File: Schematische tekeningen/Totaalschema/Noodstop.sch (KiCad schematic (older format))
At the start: 19 parts, among them J8 Noodstop, Q4 BS170, Q5 BS170, U11 PC817, U12 PC817, U13 74AHC1G32

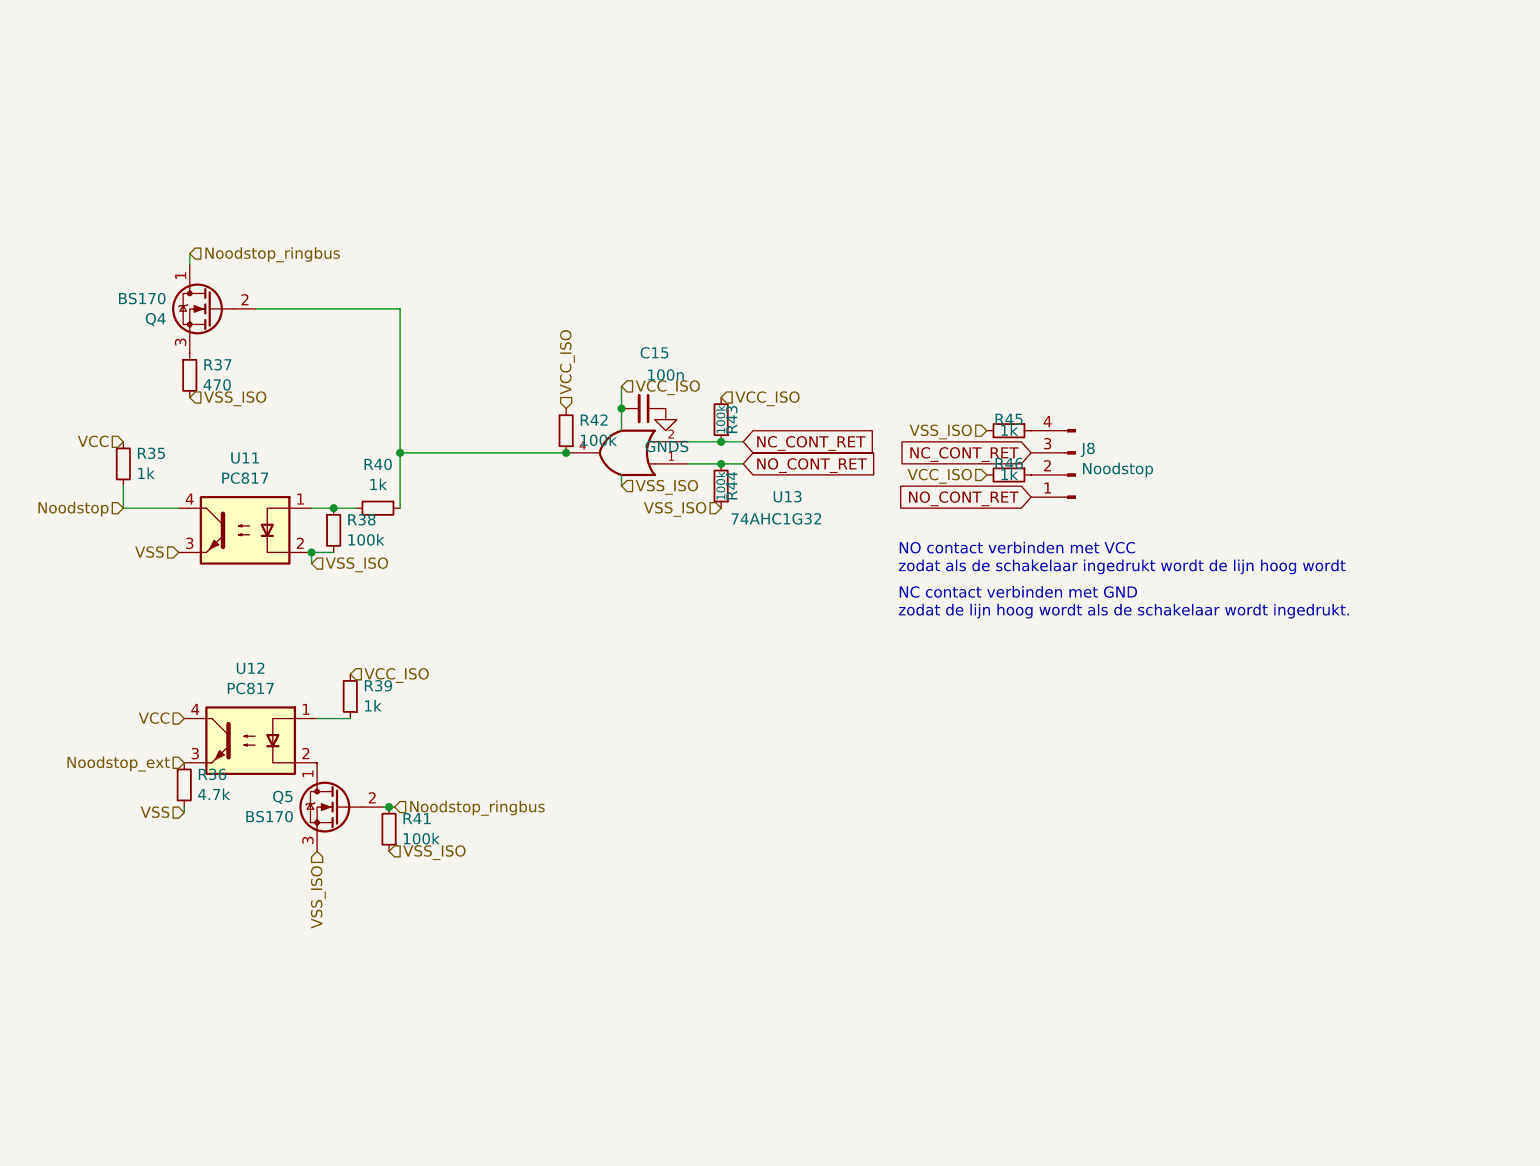
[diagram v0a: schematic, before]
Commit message: Footprints aangepast. Tekening aangepast
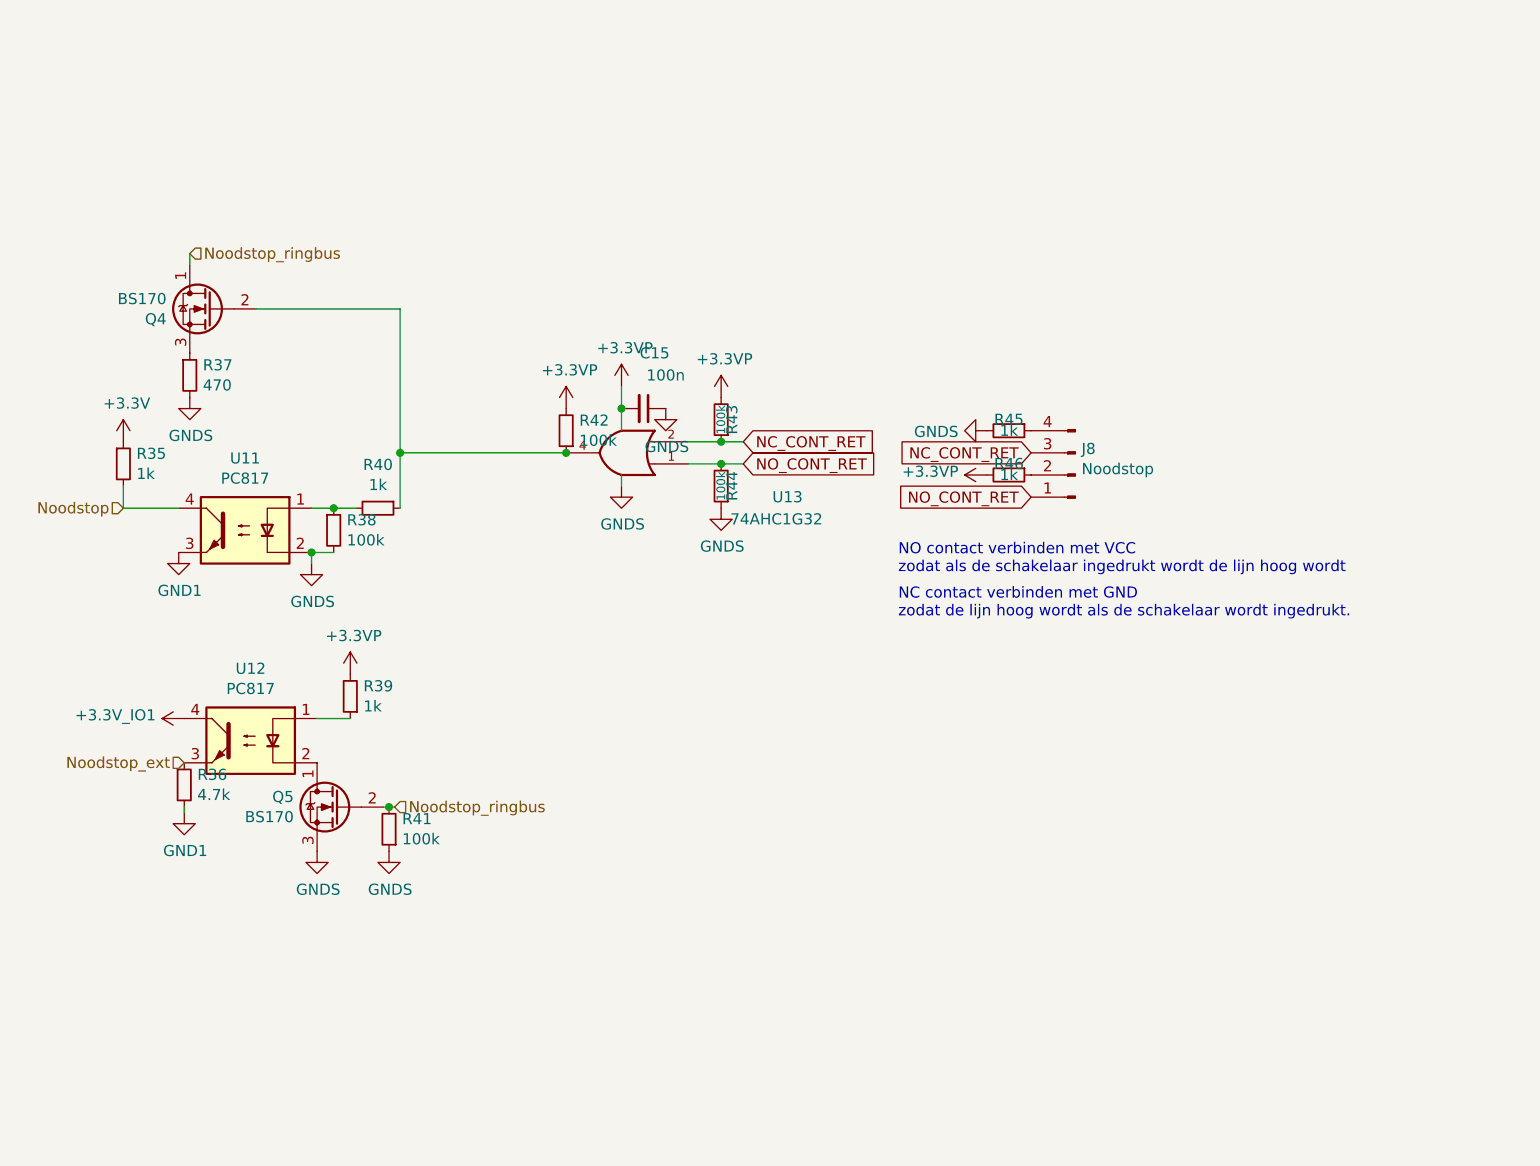
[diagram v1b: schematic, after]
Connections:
- net GNDS: now also Q5.3 (S), R37.2, R38.2, R41.1, R44.1, R45.2, U11.2, U13.5 (VCC)
- net GND renamed +3.3VP
- removed net VCC: Q5.3 (S), R35.1, R37.2, R38.2, R41.1, R44.1, R45.2, U11.2, U12.4, U13.5 (VCC)
- net VSS renamed GND1
- new net +3V3: R35.1
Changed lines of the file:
@@
 $Descr A4 11693 8268
 encoding utf-8
-Sheet 5 5
+Sheet 4 5
 Title ""
 Date ""
@@
 	0    1    1    0
 $EndComp
-Wire Wire Line
-	6250 3000 6250 3100
 Connection ~ 6250 3100
 Wire Wire Line
@@
 Text HLabel 4000 3550 0    50   Input ~ 0
 Noodstop
-Text HLabel 4250 3750 0    50   Input ~ 0
-VSS
-Text HLabel 4850 3800 2    50   Input ~ 0
-VSS_ISO
-Text HLabel 6250 3450 2    50   Input ~ 0
-VSS_ISO
 Wire Wire Line
 	6250 3450 6250 3400
-Text HLabel 6250 3000 2    50   Input ~ 0
-VCC_ISO
-Text HLabel 6700 3050 2    50   Input ~ 0
-VCC_ISO
-Text HLabel 7900 3400 0    50   Input ~ 0
-VCC_ISO
-Text HLabel 7900 3200 0    50   Input ~ 0
-VSS_ISO
-Text HLabel 4300 3050 2    50   Input ~ 0
-VSS_ISO
-Text HLabel 4000 3250 0    50   Input ~ 0
-VCC
 Text Notes 7500 3850 0    50   ~ 0
 NO contact verbinden met VCC\nzodat als de schakelaar ingedrukt wordt de lijn hoog wordt
@@
 	-1   0    0    1
 $EndComp
-Text HLabel 6000 3100 1    50   Input ~ 0
-VCC_ISO
-Text HLabel 6700 3550 0    50   Input ~ 0
-VSS_ISO
 Wire Wire Line
 	6700 3350 6550 3350
@@
 	-1   0    0    1
 $EndComp
-Text HLabel 5025 4300 2    50   Input ~ 0
-VCC_ISO
 $Comp
 L Device:R_Small R41
@@
 Wire Wire Line
 	5200 4900 5175 4900
-Text HLabel 5200 5100 2    50   Input ~ 0
-VSS_ISO
 $Comp
 L Device:R_Small R36
@@
 	1    0    0    -1
 $EndComp
-Text HLabel 4275 4500 0    50   Input ~ 0
-VCC
 Text HLabel 4275 4700 0    50   Input ~ 0
 Noodstop_ext
 Wire Wire Line
 	4275 4900 4275 4925
-Text HLabel 4275 4925 0    50   Input ~ 0
-VSS
-Text HLabel 4875 5100 3    50   Input ~ 0
-VSS_ISO
 Wire Wire Line
 	4875 4500 5025 4500
@@
 	5250 3300 6000 3300
 Connection ~ 6000 3300
+$Comp
+L power:GNDS #PWR0106
+U 1 1 61BE4256
+P 6250 3450
+F 0 "#PWR0106" H 6250 3200 50  0001 C CNN
+F 1 "GNDS" H 6255 3277 50  0000 C CNN
+F 2 "" H 6250 3450 50  0001 C CNN
+F 3 "" H 6250 3450 50  0001 C CNN
+	1    6250 3450
+	1    0    0    -1
+$EndComp
+$Comp
+L power:GNDS #PWR0110
+U 1 1 61BE48CA
+P 6700 3550
+F 0 "#PWR0110" H 6700 3300 50  0001 C CNN
+F 1 "GNDS" H 6705 3377 50  0000 C CNN
+F 2 "" H 6700 3550 50  0001 C CNN
+F 3 "" H 6700 3550 50  0001 C CNN
+	1    6700 3550
+	1    0    0    -1
+$EndComp
+Wire Wire Line
+	6250 3000 6250 3100
+$Comp
+L power:GNDS #PWR0169
+U 1 1 61BE8DD6
+P 4300 3050
+F 0 "#PWR0169" H 4300 2800 50  0001 C CNN
+F 1 "GNDS" H 4305 2877 50  0000 C CNN
+F 2 "" H 4300 3050 50  0001 C CNN
+F 3 "" H 4300 3050 50  0001 C CNN
+	1    4300 3050
+	1    0    0    -1
+$EndComp
+$Comp
+L power:GNDS #PWR0170
+U 1 1 61BEB9BE
+P 4850 3800
+F 0 "#PWR0170" H 4850 3550 50  0001 C CNN
+F 1 "GNDS" H 4855 3627 50  0000 C CNN
+F 2 "" H 4850 3800 50  0001 C CNN
+F 3 "" H 4850 3800 50  0001 C CNN
+	1    4850 3800
+	1    0    0    -1
+$EndComp
+$Comp
+L power:GND1 #PWR0171
+U 1 1 61BF1EB5
+P 4250 3750
+F 0 "#PWR0171" H 4250 3500 50  0001 C CNN
+F 1 "GND1" H 4255 3577 50  0000 C CNN
+F 2 "" H 4250 3750 50  0001 C CNN
+F 3 "" H 4250 3750 50  0001 C CNN
+	1    4250 3750
+	1    0    0    -1
+$EndComp
+$Comp
+L power:+3.3V #PWR0172
+U 1 1 61BF361B
+P 4000 3250
+F 0 "#PWR0172" H 4000 3100 50  0001 C CNN
+F 1 "+3.3V" H 4015 3423 50  0000 C CNN
+F 2 "" H 4000 3250 50  0001 C CNN
+F 3 "" H 4000 3250 50  0001 C CNN
+	1    4000 3250
+	1    0    0    -1
+$EndComp
+$Comp
+L power:GNDS #PWR0174
+U 1 1 61BF9F80
+P 5200 5100
+F 0 "#PWR0174" H 5200 4850 50  0001 C CNN
+F 1 "GNDS" H 5205 4927 50  0000 C CNN
+F 2 "" H 5200 5100 50  0001 C CNN
+F 3 "" H 5200 5100 50  0001 C CNN
+	1    5200 5100
+	1    0    0    -1
+$EndComp
+$Comp
+L power:GNDS #PWR0175
+U 1 1 61BFD78C
+P 4875 5100
+F 0 "#PWR0175" H 4875 4850 50  0001 C CNN
+F 1 "GNDS" H 4880 4927 50  0000 C CNN
+F 2 "" H 4875 5100 50  0001 C CNN
+F 3 "" H 4875 5100 50  0001 C CNN
+	1    4875 5100
+	1    0    0    -1
+$EndComp
+$Comp
+L power:GND1 #PWR0176
+U 1 1 61BFF9F4
+P 4275 4925
+F 0 "#PWR0176" H 4275 4675 50  0001 C CNN
+F 1 "GND1" H 4280 4752 50  0000 C CNN
+F 2 "" H 4275 4925 50  0001 C CNN
+F 3 "" H 4275 4925 50  0001 C CNN
+	1    4275 4925
+	1    0    0    -1
+$EndComp
+$Comp
+L eec:+3.3V_IO1 #PWR0177
+U 1 1 61C0A870
+P 4275 4500
+F 0 "#PWR0177" H 4425 4450 50  0001 C CNN
+F 1 "+3.3V_IO1" V 4290 4628 50  0000 L CNN
+F 2 "" H 4275 4500 50  0001 C CNN
+F 3 "" H 4275 4500 50  0001 C CNN
+	1    4275 4500
+	0    -1   -1   0
+$EndComp
+$Comp
+L power:GNDS #PWR0178
+U 1 1 61C0E7F5
+P 7900 3200
+F 0 "#PWR0178" H 7900 2950 50  0001 C CNN
+F 1 "GNDS" V 7905 3072 50  0000 R CNN
+F 2 "" H 7900 3200 50  0001 C CNN
+F 3 "" H 7900 3200 50  0001 C CNN
+	1    7900 3200
+	0    1    1    0
+$EndComp
+$Comp
+L power:+3.3VP #PWR0167
+U 1 1 61C3EFB9
+P 5025 4300
+F 0 "#PWR0167" H 5175 4250 50  0001 C CNN
+F 1 "+3.3VP" H 5040 4473 50  0000 C CNN
+F 2 "" H 5025 4300 50  0001 C CNN
+F 3 "" H 5025 4300 50  0001 C CNN
+	1    5025 4300
+	1    0    0    -1
+$EndComp
+$Comp
+L power:+3.3VP #PWR0168
+U 1 1 61C3FFCA
+P 6000 3100
+F 0 "#PWR0168" H 6150 3050 50  0001 C CNN
+F 1 "+3.3VP" H 6015 3273 50  0000 C CNN
+F 2 "" H 6000 3100 50  0001 C CNN
+F 3 "" H 6000 3100 50  0001 C CNN
+	1    6000 3100
+	1    0    0    -1
+$EndComp
+$Comp
+L power:+3.3VP #PWR0173
+U 1 1 61C41A5A
+P 6250 3000
+F 0 "#PWR0173" H 6400 2950 50  0001 C CNN
+F 1 "+3.3VP" H 6265 3173 50  0000 C CNN
+F 2 "" H 6250 3000 50  0001 C CNN
+F 3 "" H 6250 3000 50  0001 C CNN
+	1    6250 3000
+	1    0    0    -1
+$EndComp
+$Comp
+L power:+3.3VP #PWR0179
+U 1 1 61C42663
+P 6700 3050
+F 0 "#PWR0179" H 6850 3000 50  0001 C CNN
+F 1 "+3.3VP" H 6715 3223 50  0000 C CNN
+F 2 "" H 6700 3050 50  0001 C CNN
+F 3 "" H 6700 3050 50  0001 C CNN
+	1    6700 3050
+	1    0    0    -1
+$EndComp
+$Comp
+L power:+3.3VP #PWR0180
+U 1 1 61C42F93
+P 7900 3400
+F 0 "#PWR0180" H 8050 3350 50  0001 C CNN
+F 1 "+3.3VP" V 7915 3528 50  0000 L CNN
+F 2 "" H 7900 3400 50  0001 C CNN
+F 3 "" H 7900 3400 50  0001 C CNN
+	1    7900 3400
+	0    -1   -1   0
+$EndComp
 $EndSCHEMATC

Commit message: Totaalschema in orde maken
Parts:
- removed J8: Noodstop, Connector_PinHeader_2.54mm:PinHeader_1x04_P2.54mm_Vertical, symbol Connector:Conn_01x04_Male
- added SW?: Noodknop, symbol Switch:SW_Push_DPDT
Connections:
- net GND1 is gone; now on net +3.3VP: R36.2, U11.3
- net NC_CONT_RET: now also SW?.1 (A)
- net NO_CONT_RET: now also SW?.6 (C)
- net Noodstop_act: now reaches Q4.2 (G), R40.1, R42.1, U13.4
- net at R46.1: now also SW?.5 (B)
- net at R45.1: now also SW?.2 (B)
- no-connect marks 0 -> 2
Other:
- note removed: "NC contact verbinden met GND \nzodat de lijn hoog wordt als de schakelaar wordt ingedrukt."
- note removed: "NO contact verbinden met VCC\nzodat als de schakelaar ingedrukt wordt de lijn hoog wordt"
- moved on the sheet: C15, Q4, Q5, R35, R36, R37, R38, R39, R40, R41, R42, R43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
